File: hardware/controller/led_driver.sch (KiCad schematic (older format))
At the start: 8 parts, among them U6 IS31LT3360

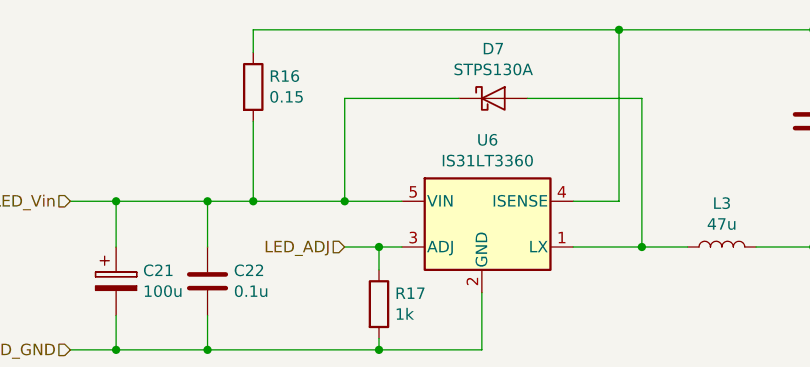
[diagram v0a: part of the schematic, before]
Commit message: initial controller components placement
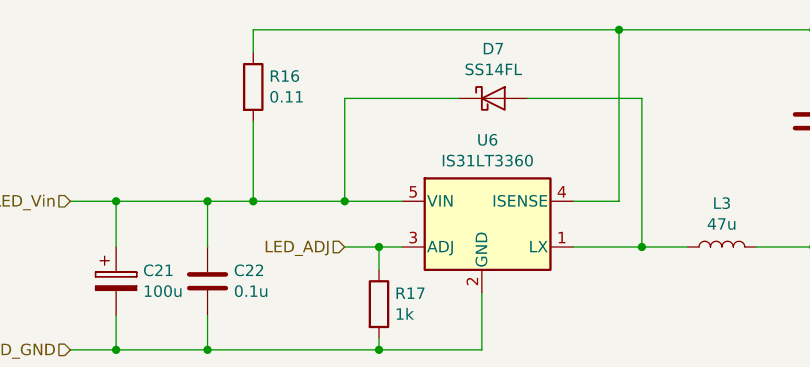
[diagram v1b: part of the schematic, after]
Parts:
- D7: value STPS130A -> SS14FL; footprint Diode_SMD:D_SMA -> Diode_SMD:D_SOD-123F
- L3: footprint Inductor_SMD:L_Bourns-SRN6028 -> led:L_12x12mm_H6mm
- R16: value 0.15 -> 0.11
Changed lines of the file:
@@
 F 0 "L3" V 7140 4100 50  0000 C CNN
 F 1 "47u" V 7049 4100 50  0000 C CNN
-F 2 "Inductor_SMD:L_Bourns-SRN6028" H 6950 4100 50  0001 C CNN
-F 3 "~" H 6950 4100 50  0001 C CNN
+F 2 "led:L_12x12mm_H6mm" H 6950 4100 50  0001 C CNN
+F 3 "https://katalog.we-online.com/pbs/datasheet/744771147.pdf" H 6950 4100 50  0001 C CNN
 	1    6950 4100
 	0    -1   -1   0
@@
 AR Path="/5BF9C747/5BF93D75" Ref="D11"  Part="1"
 F 0 "D7" H 5950 3666 50  0000 C CNN
-F 1 "STPS130A" H 5950 3575 50  0000 C CNN
-F 2 "Diode_SMD:D_SMA" H 5950 3450 50  0001 C CNN
+F 1 "SS14FL" H 5950 3575 50  0000 C CNN
+F 2 "Diode_SMD:D_SOD-123F" H 5950 3450 50  0001 C CNN
 F 3 "~" H 5950 3450 50  0001 C CNN
 	1    5950 3450
@@
 AR Path="/5BF9C747/5BF93DE8" Ref="R24"  Part="1"
 F 0 "R16" H 4970 3446 50  0000 L CNN
-F 1 "0.15" H 4970 3355 50  0000 L CNN
+F 1 "0.11" H 4970 3355 50  0000 L CNN
 F 2 "Resistor_SMD:R_0805_2012Metric_Pad1.15x1.40mm_HandSolder" V 4830 3400 50  0001 C CNN
 F 3 "~" H 4900 3400 50  0001 C CNN

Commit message: open source hardware fix
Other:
- note added: "Copyright Alexander Khoroshko 2018.\nThis documentation describes Open Hardware and is licensed under the CERN OHL v. 1.2. \nYou may redistribute and modify this documentation under the terms of the CERN OHL v.1.2. \nThis documentation is distributed WITHOUT ANY EXPRESS OR IMPLIED WARRANTY, INCLUDING \nOF MERCHANTABILITY, SATISFACTORY QUALITY AND FITNESS FOR A PARTICULAR PURPOSE. \nPlease see the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"
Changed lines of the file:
@@
 $Descr A4 11693 8268
 encoding utf-8
-Sheet 2 6
+Sheet 6 6
 Title ""
 Date ""
@@
 AR Path="/5BF9B719/5BF939D5" Ref="C30"  Part="1"
 AR Path="/5BF9C747/5BF939D5" Ref="C33"  Part="1"
-F 0 "C21" H 4418 4296 50  0000 L CNN
+F 0 "C33" H 4418 4296 50  0000 L CNN
 F 1 "100u" H 4418 4205 50  0000 L CNN
 F 2 "Capacitor_SMD:CP_Elec_10x7.9" H 4338 4100 50  0001 C CNN
@@
 AR Path="/5BF9B719/5BF93A79" Ref="C31"  Part="1"
 AR Path="/5BF9C747/5BF93A79" Ref="C34"  Part="1"
-F 0 "C22" H 4815 4296 50  0000 L CNN
+F 0 "C34" H 4815 4296 50  0000 L CNN
 F 1 "0.1u" H 4815 4205 50  0000 L CNN
 F 2 "Capacitor_SMD:C_0603_1608Metric_Pad1.05x0.95mm_HandSolder" H 4738 4100 50  0001 C CNN
@@
 AR Path="/5BF9B719/5BF93BA6" Ref="L6"  Part="1"
 AR Path="/5BF9C747/5BF93BA6" Ref="L7"  Part="1"
-F 0 "L3" V 7140 4100 50  0000 C CNN
+F 0 "L7" V 7140 4100 50  0000 C CNN
 F 1 "47u" V 7049 4100 50  0000 C CNN
 F 2 "led:L_12x12mm_H6mm" H 6950 4100 50  0001 C CNN
@@
 AR Path="/5BF9B719/5BF93C4A" Ref="C32"  Part="1"
 AR Path="/5BF9C747/5BF93C4A" Ref="C35"  Part="1"
-F 0 "C23" H 7465 3596 50  0000 L CNN
+F 0 "C35" H 7465 3596 50  0000 L CNN
 F 1 "1u" H 7465 3505 50  0000 L CNN
 F 2 "Capacitor_SMD:C_0603_1608Metric_Pad1.05x0.95mm_HandSolder" H 7388 3400 50  0001 C CNN
@@
 AR Path="/5BF9B719/5BF93D75" Ref="D10"  Part="1"
 AR Path="/5BF9C747/5BF93D75" Ref="D11"  Part="1"
-F 0 "D7" H 5950 3666 50  0000 C CNN
+F 0 "D11" H 5950 3666 50  0000 C CNN
 F 1 "SS14FL" H 5950 3575 50  0000 C CNN
 F 2 "Diode_SMD:D_SOD-123F" H 5950 3450 50  0001 C CNN
@@
 AR Path="/5BF9B719/5BF93DE8" Ref="R22"  Part="1"
 AR Path="/5BF9C747/5BF93DE8" Ref="R24"  Part="1"
-F 0 "R16" H 4970 3446 50  0000 L CNN
+F 0 "R24" H 4970 3446 50  0000 L CNN
 F 1 "0.11" H 4970 3355 50  0000 L CNN
 F 2 "Resistor_SMD:R_0805_2012Metric_Pad1.15x1.40mm_HandSolder" V 4830 3400 50  0001 C CNN
@@
 AR Path="/5BF9B719/5BF938D1" Ref="U9"  Part="1"
 AR Path="/5BF9C747/5BF938D1" Ref="U10"  Part="1"
-F 0 "U6" H 5925 4567 50  0000 C CNN
+F 0 "U10" H 5925 4567 50  0000 C CNN
 F 1 "IS31LT3360" H 5925 4476 50  0000 C CNN
 F 2 "led:SOT-89-5" H 5950 3950 50  0001 L CIN
@@
 AR Path="/5BF9B719/5BF96E51" Ref="R23"  Part="1"
 AR Path="/5BF9C747/5BF96E51" Ref="R25"  Part="1"
-F 0 "R17" H 5520 4396 50  0000 L CNN
+F 0 "R25" H 5520 4396 50  0000 L CNN
 F 1 "1k" H 5520 4305 50  0000 L CNN
 F 2 "Resistor_SMD:R_0603_1608Metric_Pad1.05x0.95mm_HandSolder" V 5380 4350 50  0001 C CNN
@@
 Wire Wire Line
 	5450 4550 5900 4550
+Text Notes 7000 7050 0    50   ~ 0
+Copyright Alexander Khoroshko 2018.\nThis   documentation   describes   Open   Hardware   and   is   licensed   under   the CERN OHL v. 1.2. \nYou may redistribute and modify this documentation under the terms of the CERN OHL v.1.2. \nThis documentation is distributed WITHOUT   ANY   EXPRESS   OR   IMPLIED   WARRANTY,   INCLUDING \nOF MERCHANTABILITY,   SATISFACTORY   QUALITY   AND   FITNESS   FOR   A PARTICULAR   PURPOSE.   \nPlease   see   the   CERN   OHL   v.1.2  for   applicable conditions.
 $EndSCHEMATC

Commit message: controller partially traced
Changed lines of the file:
@@
 $Descr A4 11693 8268
 encoding utf-8
-Sheet 6 6
+Sheet 2 6
 Title ""
 Date ""
@@
 AR Path="/5BF9B719/5BF939D5" Ref="C30"  Part="1"
 AR Path="/5BF9C747/5BF939D5" Ref="C33"  Part="1"
-F 0 "C33" H 4418 4296 50  0000 L CNN
+F 0 "C21" H 4418 4296 50  0000 L CNN
 F 1 "100u" H 4418 4205 50  0000 L CNN
 F 2 "Capacitor_SMD:CP_Elec_10x7.9" H 4338 4100 50  0001 C CNN
@@
 AR Path="/5BF9B719/5BF93A79" Ref="C31"  Part="1"
 AR Path="/5BF9C747/5BF93A79" Ref="C34"  Part="1"
-F 0 "C34" H 4815 4296 50  0000 L CNN
+F 0 "C22" H 4815 4296 50  0000 L CNN
 F 1 "0.1u" H 4815 4205 50  0000 L CNN
 F 2 "Capacitor_SMD:C_0603_1608Metric_Pad1.05x0.95mm_HandSolder" H 4738 4100 50  0001 C CNN
@@
 AR Path="/5BF9B719/5BF93BA6" Ref="L6"  Part="1"
 AR Path="/5BF9C747/5BF93BA6" Ref="L7"  Part="1"
-F 0 "L7" V 7140 4100 50  0000 C CNN
+F 0 "L3" V 7140 4100 50  0000 C CNN
 F 1 "47u" V 7049 4100 50  0000 C CNN
 F 2 "led:L_12x12mm_H6mm" H 6950 4100 50  0001 C CNN
@@
 AR Path="/5BF9B719/5BF93C4A" Ref="C32"  Part="1"
 AR Path="/5BF9C747/5BF93C4A" Ref="C35"  Part="1"
-F 0 "C35" H 7465 3596 50  0000 L CNN
+F 0 "C23" H 7465 3596 50  0000 L CNN
 F 1 "1u" H 7465 3505 50  0000 L CNN
 F 2 "Capacitor_SMD:C_0603_1608Metric_Pad1.05x0.95mm_HandSolder" H 7388 3400 50  0001 C CNN
@@
 AR Path="/5BF9B719/5BF93D75" Ref="D10"  Part="1"
 AR Path="/5BF9C747/5BF93D75" Ref="D11"  Part="1"
-F 0 "D11" H 5950 3666 50  0000 C CNN
+F 0 "D7" H 5950 3666 50  0000 C CNN
 F 1 "SS14FL" H 5950 3575 50  0000 C CNN
 F 2 "Diode_SMD:D_SOD-123F" H 5950 3450 50  0001 C CNN
@@
 AR Path="/5BF9B719/5BF93DE8" Ref="R22"  Part="1"
 AR Path="/5BF9C747/5BF93DE8" Ref="R24"  Part="1"
-F 0 "R24" H 4970 3446 50  0000 L CNN
+F 0 "R16" H 4970 3446 50  0000 L CNN
 F 1 "0.11" H 4970 3355 50  0000 L CNN
 F 2 "Resistor_SMD:R_0805_2012Metric_Pad1.15x1.40mm_HandSolder" V 4830 3400 50  0001 C CNN
@@
 AR Path="/5BF9B719/5BF938D1" Ref="U9"  Part="1"
 AR Path="/5BF9C747/5BF938D1" Ref="U10"  Part="1"
-F 0 "U10" H 5925 4567 50  0000 C CNN
+F 0 "U6" H 5925 4567 50  0000 C CNN
 F 1 "IS31LT3360" H 5925 4476 50  0000 C CNN
 F 2 "led:SOT-89-5" H 5950 3950 50  0001 L CIN
@@
 Wire Wire Line
 	7350 4100 7900 4100
-Wire Wire Line
-	7850 3150 7350 3150
 Connection ~ 6500 3150
 Wire Wire Line
@@
 AR Path="/5BF9B719/5BF96E51" Ref="R23"  Part="1"
 AR Path="/5BF9C747/5BF96E51" Ref="R25"  Part="1"
-F 0 "R25" H 5520 4396 50  0000 L CNN
+F 0 "R17" H 5520 4396 50  0000 L CNN
 F 1 "1k" H 5520 4305 50  0000 L CNN
 F 2 "Resistor_SMD:R_0603_1608Metric_Pad1.05x0.95mm_HandSolder" V 5380 4350 50  0001 C CNN
@@
 Text Notes 7000 7050 0    50   ~ 0
 Copyright Alexander Khoroshko 2018.\nThis   documentation   describes   Open   Hardware   and   is   licensed   under   the CERN OHL v. 1.2. \nYou may redistribute and modify this documentation under the terms of the CERN OHL v.1.2. \nThis documentation is distributed WITHOUT   ANY   EXPRESS   OR   IMPLIED   WARRANTY,   INCLUDING \nOF MERCHANTABILITY,   SATISFACTORY   QUALITY   AND   FITNESS   FOR   A PARTICULAR   PURPOSE.   \nPlease   see   the   CERN   OHL   v.1.2  for   applicable conditions.
+Wire Wire Line
+	7350 3150 7900 3150
 $EndSCHEMATC

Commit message: controller finished. Sent both boards for manufacturing
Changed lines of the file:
@@
 AR Path="/5BF9B719/5BF939D5" Ref="C30"  Part="1"
 AR Path="/5BF9C747/5BF939D5" Ref="C33"  Part="1"
-F 0 "C21" H 4418 4296 50  0000 L CNN
+F 0 "C27" H 4418 4296 50  0000 L CNN
 F 1 "100u" H 4418 4205 50  0000 L CNN
 F 2 "Capacitor_SMD:CP_Elec_10x7.9" H 4338 4100 50  0001 C CNN
@@
 AR Path="/5BF9B719/5BF93A79" Ref="C31"  Part="1"
 AR Path="/5BF9C747/5BF93A79" Ref="C34"  Part="1"
-F 0 "C22" H 4815 4296 50  0000 L CNN
+F 0 "C28" H 4815 4296 50  0000 L CNN
 F 1 "0.1u" H 4815 4205 50  0000 L CNN
 F 2 "Capacitor_SMD:C_0603_1608Metric_Pad1.05x0.95mm_HandSolder" H 4738 4100 50  0001 C CNN
@@
 AR Path="/5BF9B719/5BF93BA6" Ref="L6"  Part="1"
 AR Path="/5BF9C747/5BF93BA6" Ref="L7"  Part="1"
-F 0 "L3" V 7140 4100 50  0000 C CNN
+F 0 "L5" V 7140 4100 50  0000 C CNN
 F 1 "47u" V 7049 4100 50  0000 C CNN
 F 2 "led:L_12x12mm_H6mm" H 6950 4100 50  0001 C CNN
@@
 AR Path="/5BF9B719/5BF93C4A" Ref="C32"  Part="1"
 AR Path="/5BF9C747/5BF93C4A" Ref="C35"  Part="1"
-F 0 "C23" H 7465 3596 50  0000 L CNN
+F 0 "C29" H 7465 3596 50  0000 L CNN
 F 1 "1u" H 7465 3505 50  0000 L CNN
 F 2 "Capacitor_SMD:C_0603_1608Metric_Pad1.05x0.95mm_HandSolder" H 7388 3400 50  0001 C CNN
@@
 AR Path="/5BF9B719/5BF93D75" Ref="D10"  Part="1"
 AR Path="/5BF9C747/5BF93D75" Ref="D11"  Part="1"
-F 0 "D7" H 5950 3666 50  0000 C CNN
+F 0 "D9" H 5950 3666 50  0000 C CNN
 F 1 "SS14FL" H 5950 3575 50  0000 C CNN
 F 2 "Diode_SMD:D_SOD-123F" H 5950 3450 50  0001 C CNN
@@
 AR Path="/5BF9B719/5BF93DE8" Ref="R22"  Part="1"
 AR Path="/5BF9C747/5BF93DE8" Ref="R24"  Part="1"
-F 0 "R16" H 4970 3446 50  0000 L CNN
+F 0 "R20" H 4970 3446 50  0000 L CNN
 F 1 "0.11" H 4970 3355 50  0000 L CNN
 F 2 "Resistor_SMD:R_0805_2012Metric_Pad1.15x1.40mm_HandSolder" V 4830 3400 50  0001 C CNN
@@
 AR Path="/5BF9B719/5BF938D1" Ref="U9"  Part="1"
 AR Path="/5BF9C747/5BF938D1" Ref="U10"  Part="1"
-F 0 "U6" H 5925 4567 50  0000 C CNN
+F 0 "U8" H 5925 4567 50  0000 C CNN
 F 1 "IS31LT3360" H 5925 4476 50  0000 C CNN
 F 2 "led:SOT-89-5" H 5950 3950 50  0001 L CIN
@@
 AR Path="/5BF9B719/5BF96E51" Ref="R23"  Part="1"
 AR Path="/5BF9C747/5BF96E51" Ref="R25"  Part="1"
-F 0 "R17" H 5520 4396 50  0000 L CNN
+F 0 "R21" H 5520 4396 50  0000 L CNN
 F 1 "1k" H 5520 4305 50  0000 L CNN
 F 2 "Resistor_SMD:R_0603_1608Metric_Pad1.05x0.95mm_HandSolder" V 5380 4350 50  0001 C CNN
